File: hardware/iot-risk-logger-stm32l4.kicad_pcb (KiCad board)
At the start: 4 copper layers, 70 x 40 mm, 47 parts, among them J1 Conn_ARM_JTAG_SWD_10, J3 USB Type-C, Q1 IRLML6401, U1 STM32L412K8Tx, U2 W25Q64JV, U3 ST25DV04K, U4 OPT3001DNPR, U5 SHT30-DIS, U7 L78L33ABUTR, U8 LIS2DW12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

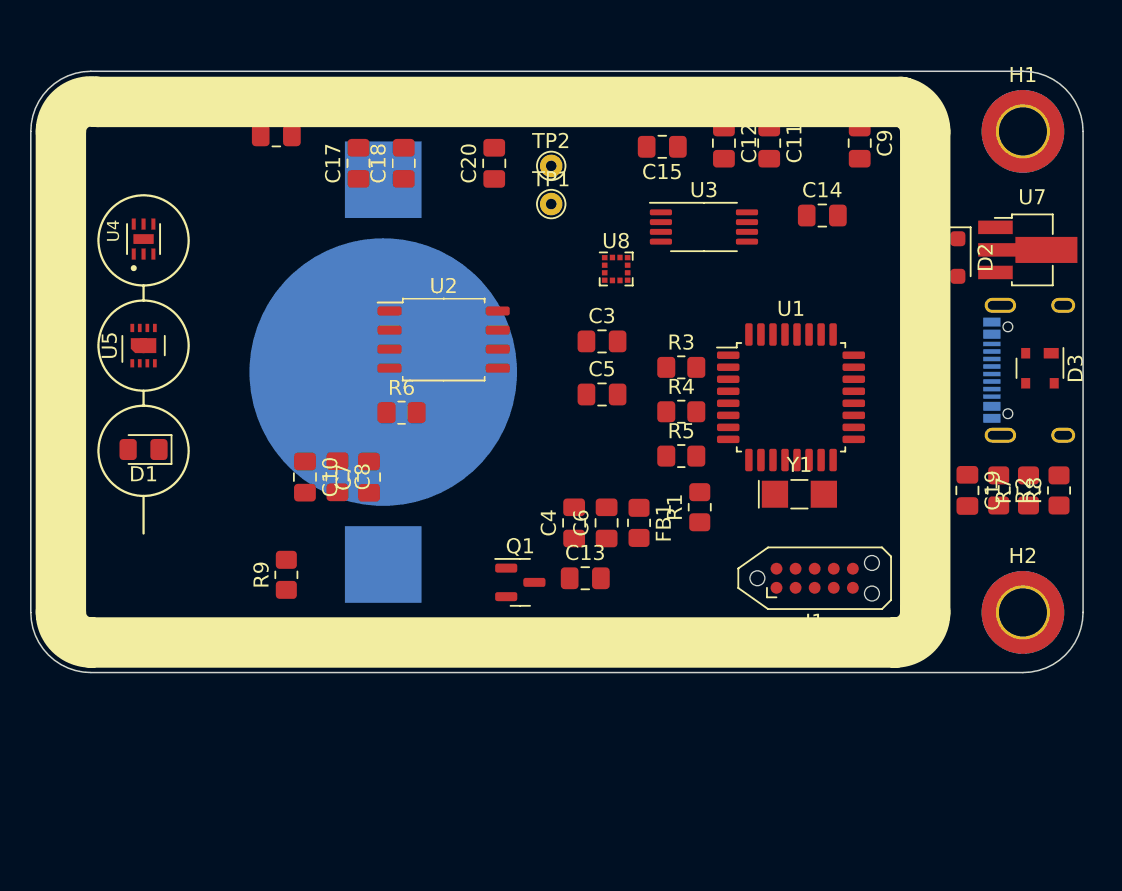
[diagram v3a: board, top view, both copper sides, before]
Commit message: PCB: first version of layout
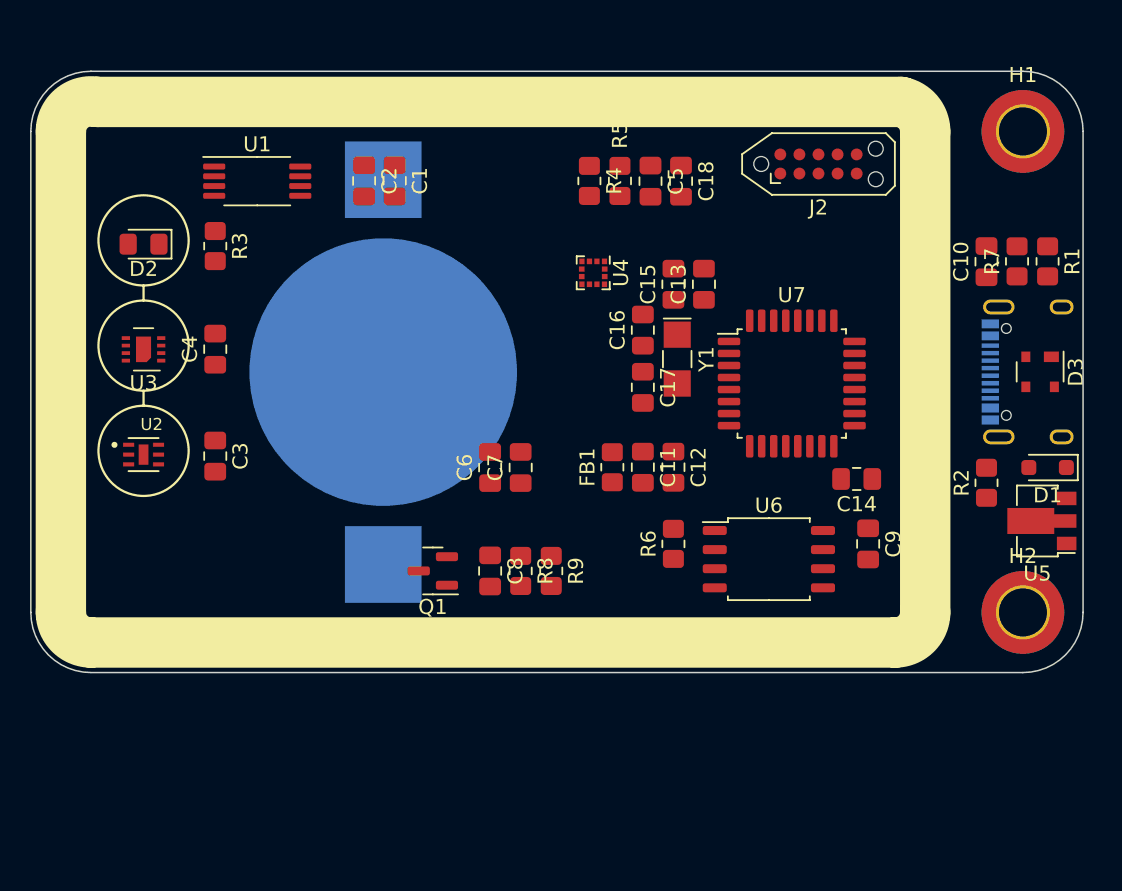
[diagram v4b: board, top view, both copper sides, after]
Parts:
- removed C19: 4n7, Capacitor_SMD:C_0805_2012Metric_Pad1.18x1.45mm_HandSolder
- removed C20: 10u, Capacitor_SMD:C_0805_2012Metric_Pad1.18x1.45mm_HandSolder
- removed J3: USB Type-C, Connector_USB:USB_C_Receptacle_XKB_U262-16XN-4BVC11
- removed TP1, TP2: TestPoint_Probe, TestPoint:TestPoint_THTPad_D1.5mm_Drill0.7mm
- removed U8: LIS2DW12, Package_LGA:LGA-12_2x2mm_P0.5mm
- added C1: 1u, Capacitor_SMD:C_0805_2012Metric_Pad1.18x1.45mm_HandSolder, F.Cu at (124.2, 67.3)
- added C16: 22p, Capacitor_SMD:C_0805_2012Metric_Pad1.18x1.45mm_HandSolder, F.Cu at (140.7, 77.2)
- added J2: Conn_ARM_JTAG_SWD_10, Connector:Tag-Connect_TC2050-IDC-NL_2x05_P1.27mm_Vertical_with_bottom_clip, F.Cu at (152.4, 66.2)
- added U6: W25Q64JV, Package_SO:SOIC-8_5.23x5.23mm_P1.27mm, F.Cu at (149.1, 92.5)
- C10: value 1u -> 4n7
- C12, C7: value 100n -> 1u
- C15, C8: value 100n -> 10u
- C18: value 22p -> 100n
- C3, C9: value 1u -> 100n
- C6: value 10u -> 100n
- D1: value LED -> BAT60A; footprint LED_SMD:LED_0805_2012Metric_Pad1.15x1.40mm_HandSolder -> Diode_SMD:D_SOD-323_HandSoldering
- D2: value BAT60A -> LED; footprint Diode_SMD:D_SOD-323_HandSoldering -> LED_SMD:LED_0805_2012Metric_Pad1.15x1.40mm_HandSolder
- J1: value Conn_ARM_JTAG_SWD_10 -> USB Type-C; footprint Connector:Tag-Connect_TC2050-IDC-NL_2x05_P1.27mm_Vertical_with_bottom_clip -> Connector_USB:USB_C_Receptacle_XKB_U262-16XN-4BVC11; moved to B.Cu
- R1: value 33k -> 5k1
- R2: value 1M -> 5k1
- R7: value 5k1 -> 1M
- R8: value 5k1 -> 82k
- R9: value 82k -> 33k
- U1: value STM32L412K8Tx -> ST25DV04K; footprint Package_QFP:LQFP-32_7x7mm_P0.8mm -> Package_SO:TSSOP-8_4.4x3mm_P0.65mm
- U2: value W25Q64JV -> OPT3001DNPR; footprint Package_SO:SOIC-8_5.23x5.23mm_P1.27mm -> Personal:SON65P200X200X65-7N
- U3: value ST25DV04K -> SHT30-DIS; footprint Package_SO:TSSOP-8_4.4x3mm_P0.65mm -> Sensor_Humidity:Sensirion_DFN-8-1EP_2.5x2.5mm_P0.5mm_EP1.1x1.7mm
- U4: value OPT3001DNPR -> LIS2DW12; footprint Personal:SON65P200X200X65-7N -> Package_LGA:LGA-12_2x2mm_P0.5mm
- U5: value SHT30-DIS -> L78L33ABUTR; footprint Sensor_Humidity:Sensirion_DFN-8-1EP_2.5x2.5mm_P0.5mm_EP1.1x1.7mm -> Package_TO_SOT_SMD:SOT-89-3
- U7: value L78L33ABUTR -> STM32L412K8Tx; footprint Package_TO_SOT_SMD:SOT-89-3_Handsoldering -> Package_QFP:LQFP-32_7x7mm_P0.8mm
- moved U5 60.6 mm to (167.0, 89.9), turned to 180 degrees
- moved D1 60.2 mm to (167.6, 86.4)
- moved D2 54.2 mm to (107.5, 71.5), turned to 180 degrees
- moved C10 47.5 mm to (163.6, 72.7), turned to 90 degrees
- moved U1 38.3 mm to (115.1, 67.3)
- moved U3 38.2 mm to (107.5, 78.5), turned to 180 degrees
- moved R8 36.2 mm to (132.6, 93.2), turned to -90 degrees
- moved R3 32.0 mm to (112.3, 71.6), turned to -90 degrees
- moved U4 30.0 mm to (137.4, 73.4), turned to -90 degrees
- moved R1 28.3 mm to (167.6, 72.6), turned to -90 degrees
- moved C3 26.8 mm to (112.3, 85.6), turned to -90 degrees
- moved C9 26.7 mm to (155.7, 91.4)
- moved C4 26.5 mm to (112.3, 78.5)
- moved C17 24.1 mm to (140.7, 81.0), turned to -90 degrees
- moved C11 23.1 mm to (140.7, 86.3)
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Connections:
- C10 pad 1: /VDDA -> Net-(D3-GND)
- C11 pad 1: +3V0 -> /VDDA
- C12 pad 1: +3V0 -> /VDDA
- C15 pad 1: _RESET -> +3V0
- C17 pad 1: Net-(U1-PC14) -> Net-(U7-PC15)
- C18 pad 1: Net-(U1-PC15) -> _RESET
- C8 pad 1: /VDDA -> +5V
- D1 pad 1: _LED -> +5V
- D2 pad 1: +5V -> _LED
- R1 pad 1: USB_VBUS_SENSE -> GND
- R1 pad 2: GND -> Net-(J1-CC1)
- R2 pad 1: Net-(D3-GND) -> GND
- R2 pad 2: GND -> Net-(J1-CC2)
- R3 pad 2: Net-(D1-A) -> Net-(D2-A)
- R4 pad 2: SCL -> SDA
- R5 pad 2: SDA -> SCL
- R7 pad 1: GND -> Net-(D3-GND)
- R7 pad 2: Net-(J3-CC1) -> GND
- R8 pad 1: GND -> +5V
- R8 pad 2: Net-(J3-CC2) -> USB_VBUS_SENSE
- R9 pad 1: +5V -> USB_VBUS_SENSE
- R9 pad 2: USB_VBUS_SENSE -> GND
- U1 pad 1: +3V0 -> unconnected-(U1-V_EH-Pad1)
- U1 pad 2: Net-(U1-PC14) -> Net-(U1-AC0)
- U1 pad 3: Net-(U1-PC15) -> Net-(U1-AC1)
- U1 pad 4: _RESET -> GND
- U1 pad 5: /VDDA -> SDA
- U1 pad 6: _NFC_INT -> SCL
- U1 pad 7: _LIGHT_INT -> _NFC_INT
- U1 pad 8: _QSPI_NCS -> +3V0
- U2 pad 1: _QSPI_NCS -> +3V0
- U2 pad 2: QSPI_IO1 -> GND
- U2 pad 3: QSPI_IO2 -> GND
- U2 pad 4: GND -> SCL
- U2 pad 5: QSPI_IO0 -> _LIGHT_INT
- U2 pad 6: QSPI_CLK -> SDA
- U2 pad 7: QSPI_IO3 -> GND
- U3 pad 1: unconnected-(U3-V_EH-Pad1) -> SDA
- U3 pad 2: Net-(U3-AC0) -> GND
- U3 pad 3: Net-(U3-AC1) -> TEMP_INT
- U3 pad 4: GND -> SCL
- U3 pad 5: SDA -> +3V0
- U3 pad 6: SCL -> _TEMP_RESET
- U3 pad 7: _NFC_INT -> GND
- U3 pad 8: +3V0 -> GND
- U4 pad 1: +3V0 -> SCL
- U4 pad 2: GND -> unconnected-(U4-~{CS}-Pad2)
- U4 pad 3: GND -> unconnected-(U4-SA0/SDO-Pad3)
- U4 pad 4: SCL -> SDA
- U4 pad 5: _LIGHT_INT -> GND
- U4 pad 6: SDA -> GND
- U5 pad 1: SDA -> +3V0
- U5 pad 3: TEMP_INT -> +5V
- U7 pad 2: GND -> Net-(U7-PC14)
- U7 pad 3: +5V -> Net-(U7-PC15)
- Y1 pad 1: Net-(U1-PC14) -> Net-(U7-PC14)
- Y1 pad 2: Net-(U1-PC15) -> Net-(U7-PC15)
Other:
- copper layers 4 -> 2

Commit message: Schematics: assign all BOM parts
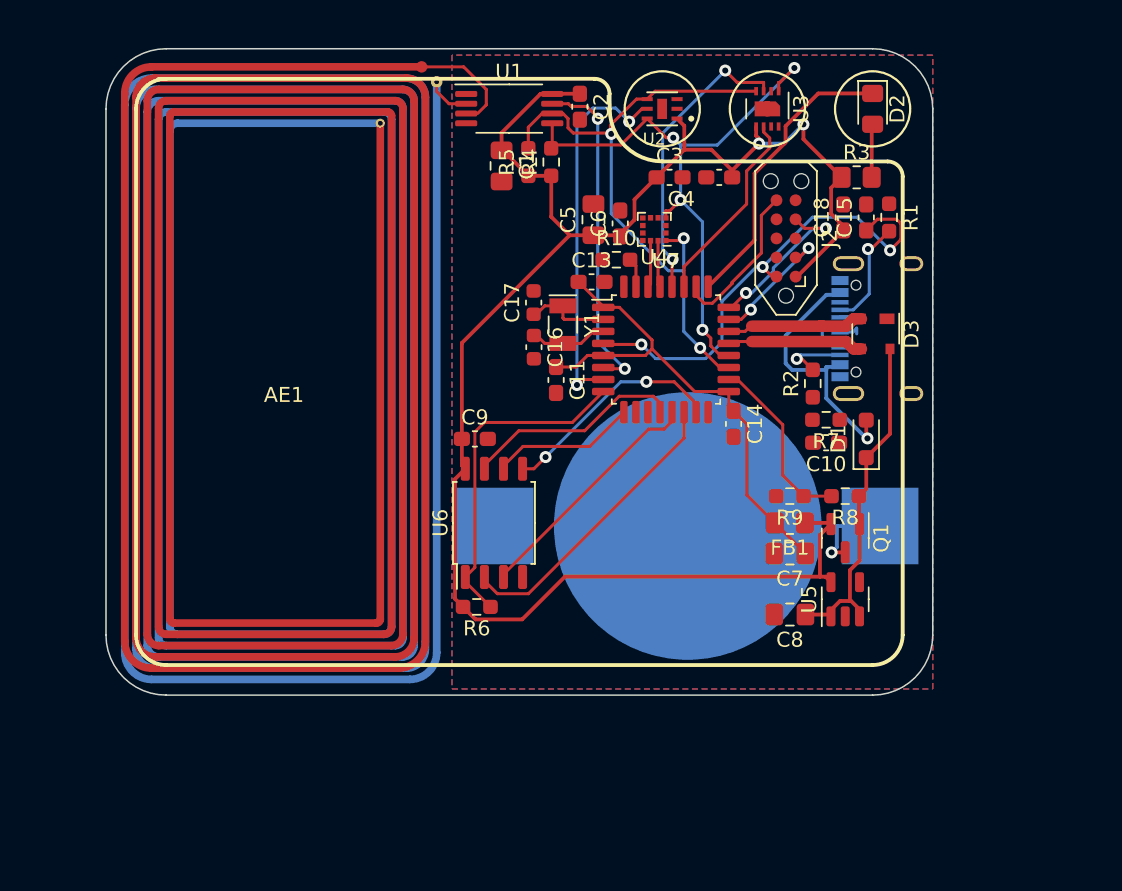
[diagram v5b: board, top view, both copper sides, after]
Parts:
- removed C12: 1u, Capacitor_SMD:C_0805_2012Metric_Pad1.18x1.45mm_HandSolder
- removed H1, H2: MountingHole, MountingHole:MountingHole_3.2mm_M3_ISO14580_Pad_TopBottom
- added AE1: Antenna_Loop, RF_Antenna:NFC_20x40, F.Cu at (116.8, 80.5)
- added R10: 10k, Resistor_SMD:R_0603_1608Metric_Pad0.98x0.95mm_HandSolder, F.Cu at (139.0, 72.5)
- C1, C7: value 1u -> 10u
- C10, C11, C13, C14, C18, C2, C3, C4, C6, C9: footprint Capacitor_SMD:C_0805_2012Metric_Pad1.18x1.45mm_HandSolder -> Capacitor_SMD:C_0603_1608Metric_Pad1.08x0.95mm_HandSolder
- C15: value 10u -> 100n; footprint Capacitor_SMD:C_0805_2012Metric_Pad1.18x1.45mm_HandSolder -> Capacitor_SMD:C_0603_1608Metric_Pad1.08x0.95mm_HandSolder
- C16, C17: footprint Capacitor_SMD:C_0805_2012Metric_Pad1.18x1.45mm_HandSolder -> Capacitor_SMD:C_0603_1608Metric
- J2: value Conn_ARM_JTAG_SWD_10 -> TagConnect SWD ARM
- R1, R2, R4, R5, R6, R7, R8, R9: footprint Resistor_SMD:R_0805_2012Metric_Pad1.20x1.40mm_HandSolder -> Resistor_SMD:R_0603_1608Metric_Pad0.98x0.95mm_HandSolder
- U5: value L78L33ABUTR -> AP2112K-3.3; footprint Package_TO_SOT_SMD:SOT-89-3 -> Package_TO_SOT_SMD:SOT-23-5
- U7: value STM32L412K8Tx -> STM32L412
- Y1: value SC-32S32.768 -> 32.768; footprint Crystal:Crystal_SMD_EuroQuartz_EQ161-2Pin_3.2x1.5mm_HandSoldering -> Crystal:Crystal_SMD_EuroQuartz_EQ161-2Pin_3.2x1.5mm
- moved D2 49.3 mm to (156.0, 62.5), turned to -90 degrees
- moved U3 44.5 mm to (149.0, 62.5), turned to -90 degrees
- moved R3 42.9 mm to (154.9, 67.1), turned to 0 degrees
- moved U2 41.5 mm to (142.0, 62.5), turned to 180 degrees
- moved C3 35.5 mm to (142.5, 67.1), turned to 0 degrees
- moved C4 35.4 mm to (145.8, 67.1), turned to 180 degrees
- moved Q1 27.5 mm to (154.2, 91.1), turned to -90 degrees
- moved C9 27.1 mm to (129.5, 84.5), turned to 0 degrees
- moved BT1 22.7 mm to (143.7, 90.2), turned to 0 degrees
- moved R8 22.2 mm to (154.2, 88.3), turned to 180 degrees
- moved C8 20.1 mm to (150.5, 96.1), turned to 180 degrees
- moved C7 18.8 mm to (150.5, 92.1), turned to 180 degrees
- moved U6 18.4 mm to (130.8, 90.0), turned to 90 degrees
- moved C6 18.4 mm to (139.2, 70.1)
- moved U1 17.4 mm to (131.8, 62.5)
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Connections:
- net Net-(BT1-+) renamed /+BATTERY
- net Net-(D1-A) renamed /+VBUS
- net Net-(D2-A) renamed /+LED
- net Net-(D3-GND) renamed /GND_SHIELD
- net Net-(J1-CC1) renamed /CC1
- net Net-(J1-CC2) renamed /CC2
- net QSPI_CLK renamed /QSPI_CLK
- net QSPI_IO0 renamed /QSPI_IO0
- net QSPI_IO1 renamed /QSPI_IO1
- net QSPI_IO2 renamed /QSPI_IO2
- net QSPI_IO3 renamed /QSPI_IO3
- net USB_DM renamed USB_N
- net USB_DP renamed USB_P
- C11 pad 1: /VDDA -> VDD
- C13 pad 1: +3V0 -> VDD
- C14 pad 1: +3V0 -> VDD
- C15 pad 1: +3V0 -> _RESET
- C16 pad 1: Net-(U7-PC14) -> /LSE_OUT
- C17 pad 1: Net-(U7-PC15) -> /LSE_IN
- C18 pad 1: _RESET -> +3V0
- C7 pad 1: +3V0 -> VDD
- FB1 pad 2: /VDDA -> VDD
- R6 pad 1: +3V0 -> /_QSPI_NCS
- R6 pad 2: _QSPI_NCS -> +3V0
- U5 pad 1: +3V0 -> +5V
- U6 pad 1: _QSPI_NCS -> /_QSPI_NCS
- U7 pad 1: +3V0 -> VDD
- U7 pad 17: +3V0 -> VDD
- U7 pad 2: Net-(U7-PC14) -> /LSE_IN
- U7 pad 3: Net-(U7-PC15) -> /LSE_OUT
- U7 pad 31: unconnected-(U7-PH3-Pad31) -> /BOOT0
- U7 pad 5: /VDDA -> VDD
- U7 pad 8: _QSPI_NCS -> /_QSPI_NCS
- Y1 pad 1: Net-(U7-PC14) -> /LSE_IN
- Y1 pad 2: Net-(U7-PC15) -> /LSE_OUT
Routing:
- net +3V0: track 0.00 -> 113.7 mm, vias 0 -> 2
- net SCL: track 0.00 -> 42.5 mm, vias 0 -> 3
- net SDA: track 0.00 -> 40.8 mm, vias 0 -> 4
- net VDD: track 0.00 -> 33.2 mm
- net _RESET: track 0.00 -> 31.9 mm, vias 0 -> 3
- net _LIGHT_INT: track 0.00 -> 25.1 mm, vias 0 -> 2
- net +5V: track 0.00 -> 22.8 mm
- net _NFC_INT: track 0.00 -> 22.3 mm, vias 0 -> 2
- net /_QSPI_NCS: track 0.00 -> 22.2 mm
- net /QSPI_IO1: track 0.00 -> 19.9 mm
- net TEMP_INT: track 0.00 -> 19.9 mm, vias 0 -> 2
- net _LED: track 0.00 -> 19.5 mm
- net /+VBUS: track 0.00 -> 18.2 mm, vias 0 -> 1
- net /QSPI_IO2: track 0.00 -> 16.2 mm
- net /QSPI_IO0: track 0.00 -> 15.1 mm, vias 0 -> 2
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- added copper zone on B.Cu, net GND
- added copper zone on F.Cu, net GND
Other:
- board size 70 x 40 mm -> 55 x 43 mm

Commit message: PCB: prefinal board
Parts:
- added G***: LOGO, LOGO, F.Cu at (116.2, 83.6)
- added REF97: WEEE-Logo_14x20mm_SilkScreen, Symbol:WEEE-Logo_14x20mm_SilkScreen, B.Cu at (116.5, 86.2)
- added REF98: OSHW-Logo_7.5x8mm_SilkScreen, Symbol:OSHW-Logo_7.5x8mm_SilkScreen, F.Cu at (116.2, 72.1)
- added REF99: KiCad-Logo2_5mm_SilkScreen, Symbol:KiCad-Logo2_5mm_SilkScreen, F.Cu at (116.3, 93.2)
- added TP1: TP: SDA, TestPoint:TestPoint_THTPad_D1.5mm_Drill0.7mm, F.Cu at (151.9, 58.8)
- added TP2: TP: SCL, TestPoint:TestPoint_THTPad_D1.5mm_Drill0.7mm, F.Cu at (146.2, 58.8)
- added TP3: TP: GND, TestPoint:TestPoint_THTPad_D1.5mm_Drill0.7mm, F.Cu at (143.6, 91.4)
- added TP4: TP: NFC_INT, TestPoint:TestPoint_THTPad_D1.5mm_Drill0.7mm, F.Cu at (137.0, 61.5)
- moved C2 7.43 mm to (129.6, 65.0), turned to 180 degrees
- moved C9 4.07 mm to (130.6, 88.4), turned to -90 degrees
- moved U6 3.63 mm to (134.2, 91.4)
- moved R1 3.33 mm to (154.6, 71.9), turned to 0 degrees
- moved FB1 2.42 mm to (150.4, 92.5), turned to 90 degrees
- moved C7 2.19 mm to (148.3, 92.5), turned to -90 degrees
- moved R8 1.91 mm to (153.0, 89.8)
- moved Q1 1.81 mm to (153.0, 92.5)
- moved C8 1.62 mm to (149.4, 97.3)
- moved U5 1.62 mm to (153.0, 96.3)
- moved C1 1.56 mm to (129.8, 66.8), turned to 180 degrees
- moved R6 1.55 mm to (130.5, 94.3), turned to 90 degrees
- moved R4 1.53 mm to (133.5, 65.0), turned to 0 degrees
- moved C15 1.31 mm to (154.4, 70.4), turned to 0 degrees
- moved BT1 1.19 mm to (143.8, 91.4)
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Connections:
- C1 pad 1: +3V0 -> VDD
- C18 pad 1: +3V0 -> VDD
- C2 pad 1: +3V0 -> VDD
- C3 pad 1: +3V0 -> VDD
- C4 pad 1: +3V0 -> VDD
- C5 pad 1: +3V0 -> VDD
- C6 pad 1: +3V0 -> VDD
- C9 pad 1: +3V0 -> VDD
- J2 pad 1: +3V0 -> VDD
- R3 pad 1: +3V0 -> VDD
- R4 pad 1: +3V0 -> VDD
- R5 pad 1: +3V0 -> VDD
- R6 pad 2: +3V0 -> VDD
- U1 pad 8: +3V0 -> VDD
- U2 pad 1: +3V0 -> VDD
- U3 pad 5: +3V0 -> VDD
- U4 pad 10: +3V0 -> VDD
- U4 pad 9: +3V0 -> VDD
- U6 pad 8: +3V0 -> VDD
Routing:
- net +3V0: track 113.7 -> 5.05 mm, vias 2 -> 0
- net VDD: track 33.2 -> 137.8 mm, vias 0 -> 3
- net /+VBUS: track 18.2 -> 0.00 mm, vias 1 -> 0
- net GND: track 0.00 -> 15.7 mm, vias 0 -> 10
- net _RESET: track 31.9 -> 20.9 mm, vias 3 -> 2
- net /QSPI_IO0: track 15.1 -> 24.6 mm
- net +5V: track 22.8 -> 29.5 mm
- net USB_P: track 12.1 -> 6.28 mm
- net SCL: track 42.5 -> 48.2 mm, vias 3 -> 2
- net /GND_SHIELD: track 0.00 -> 4.93 mm
- net /_QSPI_NCS: track 22.2 -> 17.6 mm
- net USB_N: track 11.7 -> 7.34 mm
- net /QSPI_CLK: track 9.68 -> 6.73 mm
- net SWO: track 10.5 -> 7.91 mm
- net TEMP_INT: track 19.9 -> 22.3 mm
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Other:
- board size 55 x 43 mm -> 55 x 45 mm
- board text added: "+3V"
- board text added: "+5V GND"
- board text added: "+X -X"
- board text added: "+Y-Y"
- board text added: "32K"
- board text added: "CR2032 3V"
- board text added: "FLASH"
- board text added: "GND"
- board text added: "IMU"
- board text added: "IoT NFC Logger by apolisskyi"
- board text added: "LED"
- board text added: "LIGHT"
- board text added: "NFC"
- board text added: "NFC_INT"
- board text added: "SCL"
- board text added: "SDA"
- board text added: "STM32L4 CORTEX M4"
- board text added: "T/H"
- board text added: "TODO: IMU axis"
- board text added: "TODO: LSE tracks"
- board text added: "TP: NFC_INT SCL SDA"
- board text added: "USB-C"
- board text added: "https://github.com/polesskiy-dev/iot-risk-logger-stm32l4"
- board text removed: "0"
- board text removed: "0 mm"
- board text removed: "0.0000 mm / 0.0000 mm"
- board text removed: "0.01 mm"
- board text removed: "0.02"
- board text removed: "0.035 mm"
- board text removed: "0.1 mm"
- board text removed: "0.3000 mm"
- board text removed: "1"
- board text removed: "1.24 mm"
- board text removed: "1.6000 mm"
- board text removed: "3.3"
- board text removed: "4"
- board text removed: "4.5"
- board text removed: "70.0000 mm x 40.0000 mm"
- board text removed: "B.Cu"
- board text removed: "B.Mask"
- board text removed: "B.Paste"
- board text removed: "B.Silkscreen"
- board text removed: "BOARD CHARACTERISTICS"
- board text removed: "Board Thickness:"
- board text removed: "Board overall dimensions:"
- board text removed: "Bottom Silk Screen"
- board text removed: "Bottom Solder Mask"
- board text removed: "Bottom Solder Paste"
- board text removed: "Castellated pads:"
- board text removed: "Color"
- board text removed: "Copper Finish:"
- board text removed: "Copper Layer Count:"
- board text removed: "Dielectric 1"
- board text removed: "Dielectric 2"
- board text removed: "Dielectric 3"
- board text removed: "Edge card connectors:"
- board text removed: "Epsilon R"
- board text removed: "F.Cu"
- board text removed: "F.Mask"
- board text removed: "F.Paste"
- board text removed: "F.Silkscreen"
- board text removed: "FR4"
- board text removed: "FR4 natural"
- board text removed: "Impedance Control:"
- board text removed: "In1.Cu"
- board text removed: "In2.Cu"
- board text removed: "Layer Name"
- board text removed: "Loss Tangent"
- board text removed: "Material"
- board text removed: "Min hole diameter:"
- board text removed: "Min track/spacing:"
- board text removed: "No"
- board text removed: "None"
- board text removed: "Not specified"
- board text removed: "Plated Board Edge:"
- board text removed: "Red"
- board text removed: "Thickness (mm)"
- board text removed: "Top Silk Screen"
- board text removed: "Top Solder Mask"
- board text removed: "Top Solder Paste"
- board text removed: "Type"
- board text removed: "White"
- board text removed: "copper"
- board text removed: "core"
- board text removed: "prepreg"

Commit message: PCB: prefinal static routing
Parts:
- added TP3: TP: GND, TestPoint:TestPoint_THTPad_D1.5mm_Drill0.7mm, F.Cu at (143.6, 91.4)
- moved D3 0.38 mm to (154.9, 78.0)
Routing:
- net VDD: track 137.8 -> 8.16 mm, vias 3 -> 0
- net SCL: track 48.2 -> 0.00 mm, vias 2 -> 0
- net SDA: track 41.7 -> 0.00 mm, vias 2 -> 0
- net +5V: track 29.5 -> 0.00 mm
- net /QSPI_IO0: track 24.6 -> 0.00 mm, vias 2 -> 0
- net _NFC_INT: track 23.8 -> 0.00 mm, vias 1 -> 0
- net _LIGHT_INT: track 22.9 -> 0.00 mm, vias 2 -> 0
- net TEMP_INT: track 22.3 -> 0.00 mm, vias 2 -> 0
- net _RESET: track 20.9 -> 0.00 mm, vias 2 -> 0
- net _LED: track 20.2 -> 0.00 mm, vias 2 -> 0
- net /QSPI_IO1: track 19.7 -> 0.00 mm
- net /_QSPI_NCS: track 17.6 -> 0.00 mm
- net /QSPI_IO2: track 15.2 -> 0.00 mm
- net _TEMP_RESET: track 14.2 -> 0.00 mm
- net /QSPI_IO3: track 13.3 -> 0.00 mm, vias 2 -> 0
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
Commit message: PCB: routed
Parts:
- removed the TP3 at (143.6, 91.4)
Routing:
- net VDD: track 8.16 -> 139.4 mm, vias 0 -> 4
- net SDA: track 0.00 -> 59.0 mm, vias 0 -> 3
- net SCL: track 0.00 -> 46.7 mm, vias 0 -> 2
- net +5V: track 0.00 -> 29.0 mm
- net _LIGHT_INT: track 0.00 -> 23.7 mm, vias 0 -> 2
- net _NFC_INT: track 0.00 -> 23.3 mm, vias 0 -> 1
- net /QSPI_IO1: track 0.00 -> 22.1 mm, vias 0 -> 2
- net _RESET: track 0.00 -> 21.3 mm, vias 0 -> 2
- net TEMP_INT: track 0.00 -> 19.8 mm, vias 0 -> 2
- net _LED: track 0.00 -> 19.8 mm, vias 0 -> 2
- net /_QSPI_NCS: track 0.00 -> 17.6 mm
- net /QSPI_IO2: track 0.00 -> 17.5 mm
- net /+VBUS: track 0.00 -> 14.9 mm, vias 0 -> 1
- net _TEMP_RESET: track 0.00 -> 14.5 mm, vias 0 -> 2
- net /QSPI_IO3: track 0.00 -> 14.2 mm, vias 0 -> 2
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- added copper zone on F.Cu, net VDD
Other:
- board text removed: "TODO: IMU axis"
- board text removed: "TODO: LSE tracks"
